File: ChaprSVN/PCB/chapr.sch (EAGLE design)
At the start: 30 parts, among them M2 RN42 Module, T1 3906, T2 3904

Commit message: Added power monitoring resistors. Fixed R15 label. Bumped to v1.1
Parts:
- removed C1, C2: (no value), resistor:CPOL-USE2.5-5
- added R16, R17: 24K, resistor:R-US_0207/10
- R15: value 10k -> 1.5k
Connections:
- new net N$31: ARDUINO.A6, R16.1, R17.2
- net +5V: no longer C1.+
- net GND: now also R16.2; no longer C1.-, C2.-
- net N$23: now also R17.1; no longer C2.+
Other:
- note added: "Power Monitor => A6"
- note added: "V 1.1"
- note removed: "V 1.0"
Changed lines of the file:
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@@
 <part name="R13" library="resistor" deviceset="R-US_" device="0207/10" value="10k"/>
 <part name="R14" library="resistor" deviceset="R-US_" device="0207/10" value="19.1k"/>
-<part name="R15" library="resistor" deviceset="R-US_" device="0207/10" value="10k"/>
+<part name="R15" library="resistor" deviceset="R-US_" device="0207/10" value="1.5k"/>
 <part name="D1" library="diode" deviceset="1N4148" device="DO35-7" value="1N4148"/>
 <part name="D2" library="diode" deviceset="1N4148" device="DO35-7" value="1N4148"/>
@@
 <part name="GND8" library="supply1" deviceset="GND" device=""/>
 <part name="U$3" library="ChapR-Custom" deviceset="VDIP2" device="BIGHOLE"/>
-<part name="C1" library="resistor" deviceset="CPOL-US" device="E2.5-5"/>
-<part name="C2" library="resistor" deviceset="CPOL-US" device="E2.5-5"/>
 <part name="GND9" library="supply1" deviceset="GND" device=""/>
-<part name="GND10" library="supply1" deviceset="GND" device=""/>
 <part name="T1" library="transistor-neu-to92" deviceset="*-PNP-" device="TO92-EBC" value="3906"/>
 <part name="T2" library="transistor-neu-to92" deviceset="*-NPN-" device="TO92-EBC" value="3904"/>
+<part name="R17" library="resistor" deviceset="R-US_" device="0207/10" value="24K"/>
+<part name="R16" library="resistor" deviceset="R-US_" device="0207/10" value="24K"/>
 </parts>
 <sheets>
@@
 <text x="81.026" y="18.796" size="1.778" layer="91">UART_TO_RN42</text>
 <text x="60.96" y="68.58" size="1.778" layer="91">UART_FROM_RN42</text>
-<text x="32.512" y="71.374" size="1.778" layer="91">Reset</text>
+<text x="45.212" y="71.374" size="1.778" layer="91">Reset</text>
 <wire x1="-83.82" y1="-30.48" x2="25.4" y2="-30.48" width="0.1524" layer="97"/>
 <wire x1="25.4" y1="-30.48" x2="25.4" y2="-76.2" width="0.1524" layer="97"/>
@@
 <text x="121.92" y="91.44" size="1.778" layer="97">*</text>
 <text x="111.506" y="125.222" size="1.778" layer="97">NOTE: 3.3v Comes from VDIP not ARD</text>
-<text x="162.56" y="-68.58" size="2.54" layer="97">V 1.0</text>
+<text x="162.56" y="-68.58" size="2.54" layer="97">V 1.1</text>
 <text x="76.2" y="-48.26" size="2.54" layer="97">ChapR Board</text>
-<text x="-5.08" y="-43.18" size="1.778" layer="97">Button  =&gt;  A0</text>
-<text x="-5.08" y="-48.26" size="1.778" layer="97">Speaker  &lt;=  A3</text>
-<text x="-5.08" y="-53.34" size="1.778" layer="97">Connect LED  &lt;=  A1</text>
-<text x="-5.08" y="-58.42" size="1.778" layer="97">Power LED  &lt;=  A2</text>
+<text x="-5.08" y="-37.338" size="1.778" layer="97">Button  =&gt;  A0</text>
+<text x="-5.08" y="-42.418" size="1.778" layer="97">Speaker  &lt;=  A3</text>
+<text x="-5.08" y="-47.498" size="1.778" layer="97">Connect LED  &lt;=  A1</text>
+<text x="-5.08" y="-52.578" size="1.778" layer="97">Power LED  &lt;=  A2</text>
 <text x="111.76" y="5.08" size="1.778" layer="91">Connected</text>
 <text x="4.318" y="125.476" size="1.778" layer="91" rot="R180">+</text>
@@
 <text x="49.022" y="79.502" size="1.778" layer="91">PowerHold</text>
 <text x="39.878" y="89.662" size="1.778" layer="91" rot="R90">SwitchMonitor</text>
-<text x="-5.08" y="-63.5" size="1.778" layer="97">Power Switch Mon =&gt; A5</text>
-<text x="-5.08" y="-66.548" size="1.778" layer="97">Power OFF &lt;= A4</text>
+<text x="-5.08" y="-57.658" size="1.778" layer="97">Power Switch Mon =&gt; A5</text>
+<text x="-5.334" y="-62.992" size="1.778" layer="97">Power OFF &lt;= A4</text>
 <text x="43.434" y="87.376" size="1.778" layer="91" rot="R90">(req's SW pull-up)</text>
+<text x="-5.588" y="-68.326" size="1.778" layer="95">Power Monitor =&gt; A6</text>
 </plain>
 <instances>
@@
 <instance part="ARDUINO" gate="G$1" x="2.54" y="55.88"/>
 <instance part="SUPPLY2" gate="G$1" x="-2.54" y="129.54"/>
-<instance part="GND4" gate="1" x="0" y="-12.7"/>
+<instance part="GND4" gate="1" x="-5.08" y="-10.16"/>
 <instance part="R9" gate="G$1" x="-50.8" y="2.54"/>
 <instance part="GND7" gate="1" x="-55.88" y="-20.32"/>
@@
 <instance part="GND8" gate="1" x="66.04" y="83.82"/>
 <instance part="U$3" gate="G$1" x="-55.88" y="50.8"/>
-<instance part="C1" gate="G$1" x="-33.02" y="124.46"/>
-<instance part="C2" gate="G$1" x="96.52" y="104.14"/>
-<instance part="GND9" gate="1" x="-25.4" y="114.3"/>
-<instance part="GND10" gate="1" x="96.52" y="96.52"/>
+<instance part="GND9" gate="1" x="35.56" y="-40.64"/>
 <instance part="T1" gate="G$1" x="83.82" y="114.3" smashed="yes">
 <attribute name="NAME" x="88.9" y="114.3" size="1.778" layer="95"/>
@@
 <attribute name="NAME" x="68.58" y="91.44" size="1.778" layer="95" rot="MR180"/>
 <attribute name="VALUE" x="68.58" y="93.98" size="1.778" layer="96" rot="MR180"/>
+</instance>
+<instance part="R17" gate="G$1" x="35.56" y="-7.62" smashed="yes" rot="R270">
+<attribute name="NAME" x="31.9786" y="-6.35" size="1.778" layer="95" rot="R270"/>
+<attribute name="VALUE" x="37.338" y="-6.35" size="1.778" layer="96" rot="R270"/>
+</instance>
+<instance part="R16" gate="G$1" x="35.56" y="-27.94" smashed="yes" rot="R270">
+<attribute name="NAME" x="31.9786" y="-26.67" size="1.778" layer="95" rot="R270"/>
+<attribute name="VALUE" x="37.338" y="-26.67" size="1.778" layer="96" rot="R270"/>
 </instance>
 </instances>
@@
 <wire x1="-12.7" y1="60.96" x2="-25.4" y2="60.96" width="0.1524" layer="91"/>
 <wire x1="-25.4" y1="60.96" x2="-25.4" y2="-5.08" width="0.1524" layer="91"/>
-<wire x1="-25.4" y1="-5.08" x2="0" y2="-5.08" width="0.1524" layer="91"/>
+<wire x1="-25.4" y1="-5.08" x2="-5.08" y2="-5.08" width="0.1524" layer="91"/>
 <pinref part="GND4" gate="1" pin="GND"/>
-<wire x1="0" y1="-5.08" x2="0" y2="-10.16" width="0.1524" layer="91"/>
-<junction x="0" y="-5.08"/>
+<wire x1="-5.08" y1="-5.08" x2="-5.08" y2="-7.62" width="0.1524" layer="91"/>
+<junction x="-5.08" y="-5.08"/>
 <pinref part="R10" gate="G$1" pin="1"/>
 <wire x1="27.94" y1="7.62" x2="27.94" y2="-5.08" width="0.1524" layer="91"/>
 <wire x1="27.94" y1="-5.08" x2="25.4" y2="-5.08" width="0.1524" layer="91"/>
 <pinref part="ARDUINO" gate="G$1" pin="GND2"/>
-<wire x1="25.4" y1="-5.08" x2="0" y2="-5.08" width="0.1524" layer="91"/>
+<wire x1="25.4" y1="-5.08" x2="-5.08" y2="-5.08" width="0.1524" layer="91"/>
 <wire x1="15.24" y1="66.04" x2="25.4" y2="66.04" width="0.1524" layer="91"/>
 <wire x1="25.4" y1="66.04" x2="25.4" y2="-5.08" width="0.1524" layer="91"/>
@@
 </segment>
 <segment>
-<pinref part="C1" gate="G$1" pin="-"/>
-<wire x1="-33.02" y1="119.38" x2="-25.4" y2="119.38" width="0.1524" layer="91"/>
 <pinref part="GND9" gate="1" pin="GND"/>
-<wire x1="-25.4" y1="119.38" x2="-25.4" y2="116.84" width="0.1524" layer="91"/>
-</segment>
-<segment>
-<pinref part="C2" gate="G$1" pin="-"/>
-<pinref part="GND10" gate="1" pin="GND"/>
+<pinref part="R16" gate="G$1" pin="2"/>
+<wire x1="35.56" y1="-38.1" x2="35.56" y2="-33.02" width="0.1524" layer="91"/>
 </segment>
 </net>
@@
 <pinref part="M2" gate="G$1" pin="UARTTX"/>
 <wire x1="106.68" y1="68.58" x2="101.6" y2="68.58" width="0.1524" layer="91"/>
-<wire x1="101.6" y1="68.58" x2="33.02" y2="68.58" width="0.1524" layer="91"/>
-<wire x1="33.02" y1="68.58" x2="33.02" y2="45.72" width="0.1524" layer="91"/>
+<wire x1="101.6" y1="68.58" x2="38.1" y2="68.58" width="0.1524" layer="91"/>
+<wire x1="38.1" y1="68.58" x2="38.1" y2="45.72" width="0.1524" layer="91"/>
 <pinref part="ARDUINO" gate="G$1" pin="D12"/>
-<wire x1="33.02" y1="45.72" x2="15.24" y2="45.72" width="0.1524" layer="91"/>
+<wire x1="38.1" y1="45.72" x2="15.24" y2="45.72" width="0.1524" layer="91"/>
 </segment>
 </net>
@@
 <pinref part="U$3" gate="G$1" pin="5.0V(2)"/>
 <pinref part="U$3" gate="G$1" pin="5.0V(3)"/>
-<wire x1="-33.02" y1="127" x2="-43.18" y2="127" width="0.1524" layer="91"/>
-<junction x="-43.18" y="127"/>
-<pinref part="C1" gate="G$1" pin="+"/>
 </segment>
 </net>
@@
 <segment>
 <pinref part="ARDUINO" gate="G$1" pin="RAWV"/>
-<wire x1="17.78" y1="76.2" x2="17.78" y2="68.58" width="0.1524" layer="91"/>
-<wire x1="17.78" y1="68.58" x2="15.24" y2="68.58" width="0.1524" layer="91"/>
+<wire x1="35.56" y1="76.2" x2="35.56" y2="68.58" width="0.1524" layer="91"/>
+<wire x1="35.56" y1="68.58" x2="15.24" y2="68.58" width="0.1524" layer="91"/>
 <wire x1="86.36" y1="109.22" x2="86.36" y2="106.68" width="0.1524" layer="91"/>
 <wire x1="86.36" y1="106.68" x2="86.36" y2="76.2" width="0.1524" layer="91"/>
-<wire x1="86.36" y1="76.2" x2="17.78" y2="76.2" width="0.1524" layer="91"/>
-<pinref part="C2" gate="G$1" pin="+"/>
-<wire x1="96.52" y1="106.68" x2="86.36" y2="106.68" width="0.1524" layer="91"/>
-<junction x="86.36" y="106.68"/>
+<wire x1="86.36" y1="76.2" x2="35.56" y2="76.2" width="0.1524" layer="91"/>
 <pinref part="T1" gate="G$1" pin="C"/>
+<junction x="35.56" y="68.58"/>
+<pinref part="R17" gate="G$1" pin="1"/>
+<wire x1="35.56" y1="68.58" x2="35.56" y2="-2.54" width="0.1524" layer="91"/>
 </segment>
 </net>
@@
 </segment>
 </net>
+<net name="N$31" class="0">
+<segment>
+<pinref part="ARDUINO" gate="G$1" pin="A6"/>
+<wire x1="2.54" y1="25.4" x2="2.54" y2="-12.7" width="0.1524" layer="91"/>
+<wire x1="2.54" y1="-12.7" x2="20.32" y2="-12.7" width="0.1524" layer="91"/>
+<pinref part="R17" gate="G$1" pin="2"/>
+<wire x1="20.32" y1="-12.7" x2="35.56" y2="-12.7" width="0.1524" layer="91"/>
+<junction x="35.56" y="-12.7"/>
+<pinref part="R16" gate="G$1" pin="1"/>
+<wire x1="35.56" y1="-12.7" x2="35.56" y2="-22.86" width="0.1524" layer="91"/>
+</segment>
+</net>

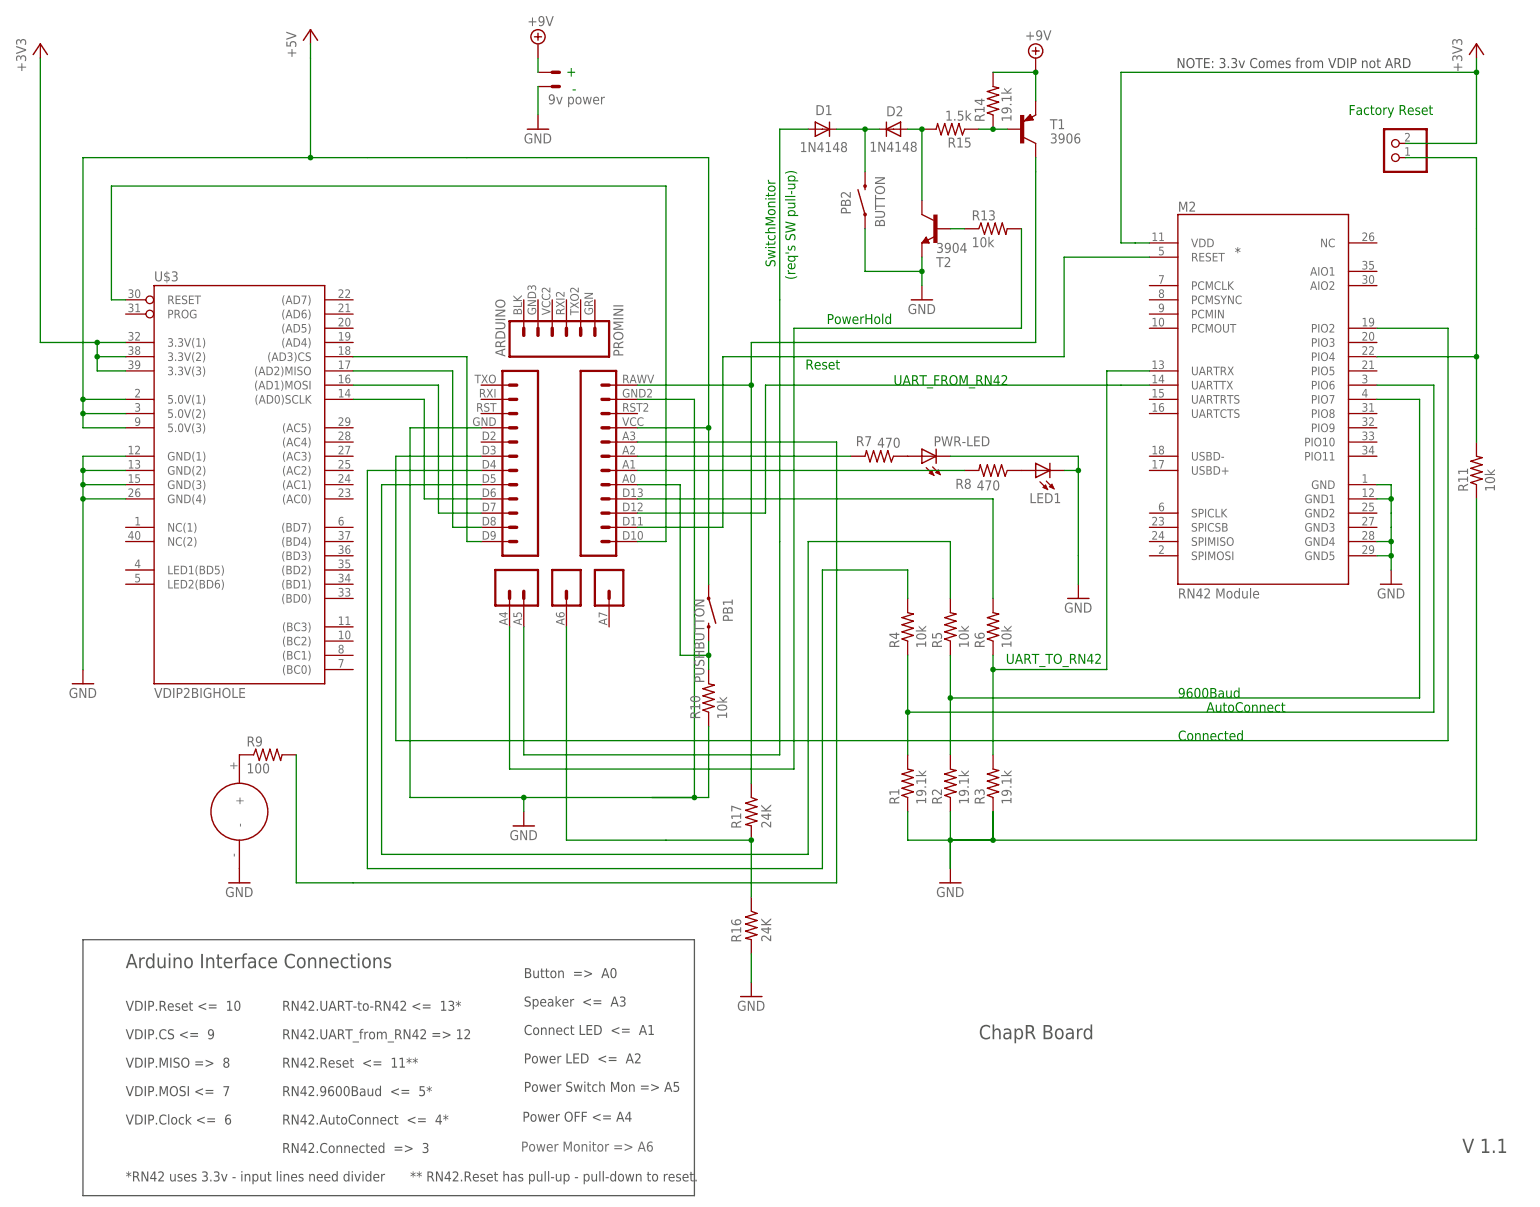
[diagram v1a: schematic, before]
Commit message: 
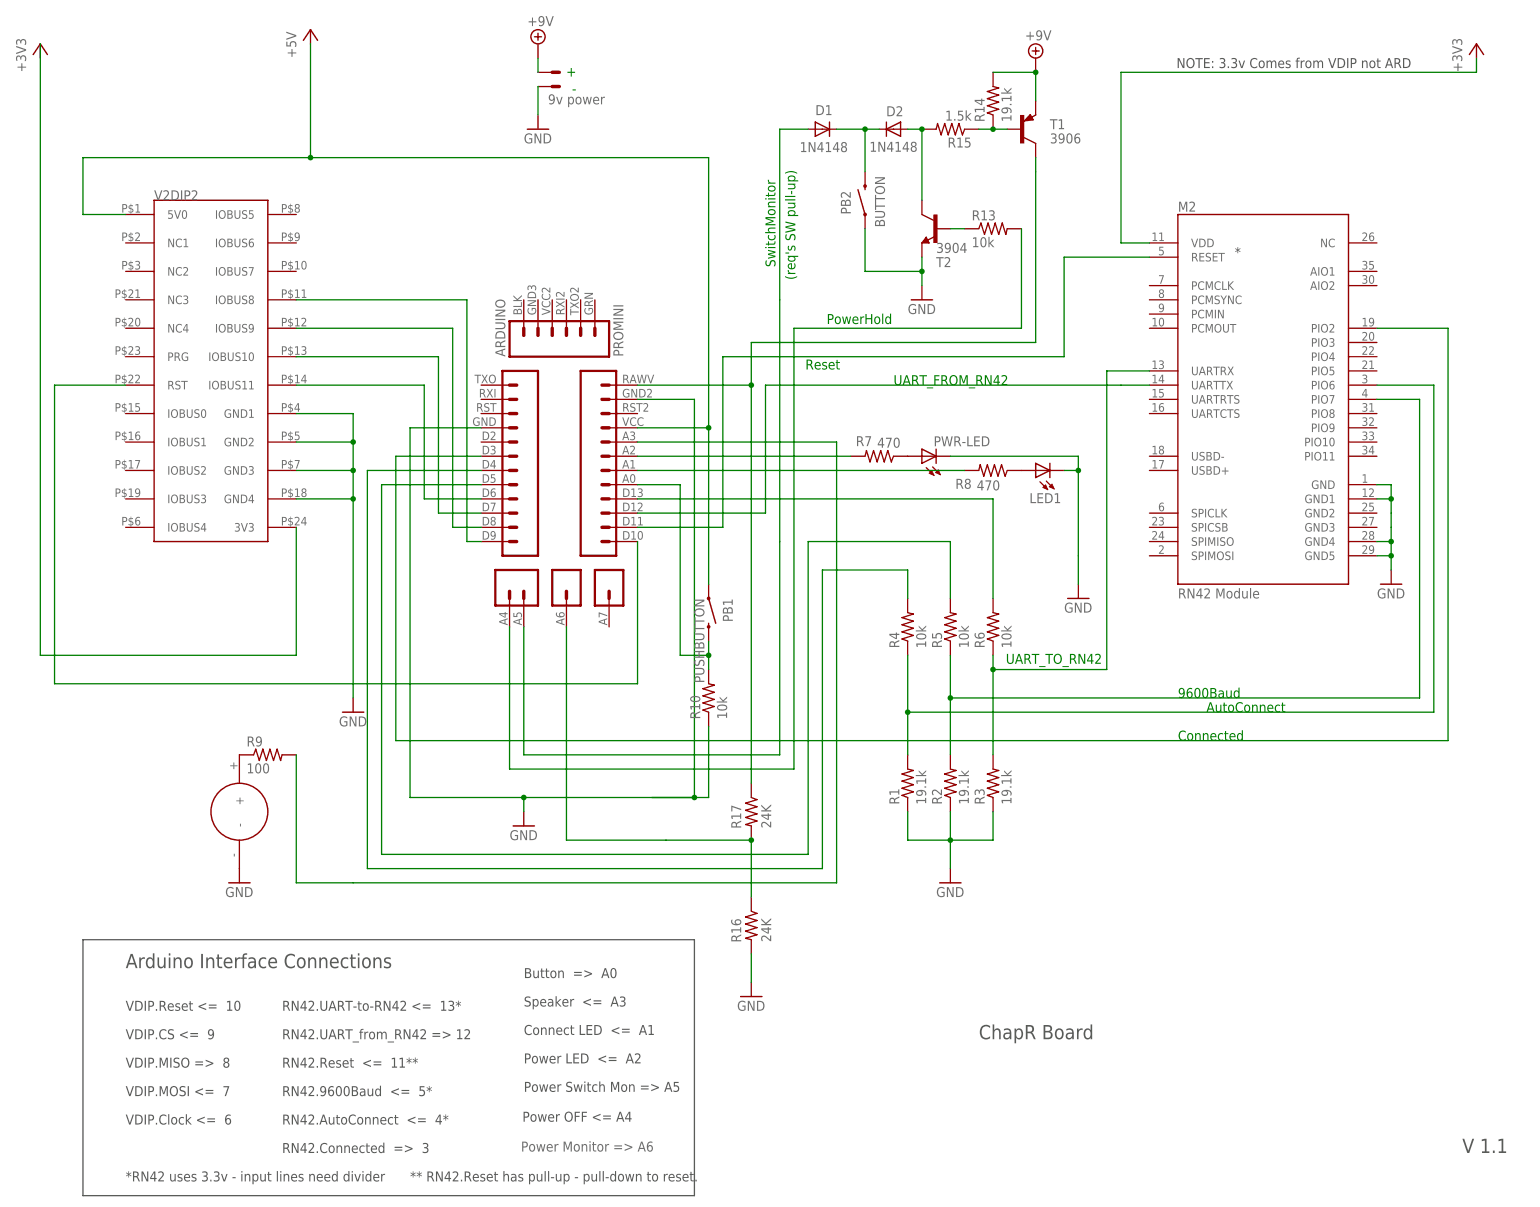
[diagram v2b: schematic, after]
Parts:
- removed JP1: (no value), pinhead:PINHD-1X2
- removed R11: 10k, resistor:R-US_0207/10
- removed U$3: VDIP2BIGHOLE, ChapR-Custom:VDIP2BIGHOLE
- added V2DIP2: V2DIP2, ChapR-Custom:V2DIP2
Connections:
- removed net N$22: JP1.1, M2.PIO4, R11.2
- new net N$28: V2DIP2.3V3
- net +3V3: no longer JP1.2, U$3.3.3V(1), U$3.3.3V(2), U$3.3.3V(3)
- net +5V: now also V2DIP2.5V0; no longer U$3.5.0V(1), U$3.5.0V(2), U$3.5.0V(3)
- net GND: now also V2DIP2.GND1, V2DIP2.GND2, V2DIP2.GND3, V2DIP2.GND4; no longer R11.1, U$3.GND(1), U$3.GND(2), U$3.GND(3), U$3.GND(4)
- net N$10: now also ARDUINO.D6, V2DIP2.IOBUS11; no longer ARDUINO.D9, U$3.(AD3)CS
- net N$11: now also ARDUINO.D7, V2DIP2.IOBUS10; no longer ARDUINO.D8, U$3.(AD2)MISO
- net N$12: now also ARDUINO.D8, V2DIP2.IOBUS9; no longer ARDUINO.D7, U$3.(AD1)MOSI
- net N$13: now also ARDUINO.D9, V2DIP2.IOBUS8; no longer ARDUINO.D6, U$3.(AD0)SCLK
- net N$2: now also V2DIP2.RST; no longer U$3.RESET
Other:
- note removed: "Factory Reset"

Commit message: 
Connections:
- removed net N$28: V2DIP2.3V3
- net +3V3: now also V2DIP2.3V3
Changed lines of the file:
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@@
 <wire x1="165.1" y1="124.46" x2="165.1" y2="127" width="0.1524" layer="91"/>
+</segment>
+<segment>
+<wire x1="-91.44" y1="129.54" x2="-91.44" y2="20.32" width="0.1524" layer="91"/>
+<wire x1="-91.44" y1="20.32" x2="-45.72" y2="20.32" width="0.1524" layer="91"/>
+<pinref part="V2DIP2" gate="G$1" pin="3V3"/>
+<wire x1="-45.72" y1="20.32" x2="-45.72" y2="43.18" width="0.1524" layer="91"/>
 </segment>
 </net>
@@
 </segment>
 </net>
-<net name="N$28" class="0">
-<segment>
-<wire x1="-91.44" y1="129.54" x2="-91.44" y2="20.32" width="0.1524" layer="91"/>
-<wire x1="-91.44" y1="20.32" x2="-45.72" y2="20.32" width="0.1524" layer="91"/>
-<pinref part="V2DIP2" gate="G$1" pin="3V3"/>
-<wire x1="-45.72" y1="20.32" x2="-45.72" y2="43.18" width="0.1524" layer="91"/>
-</segment>
-</net>

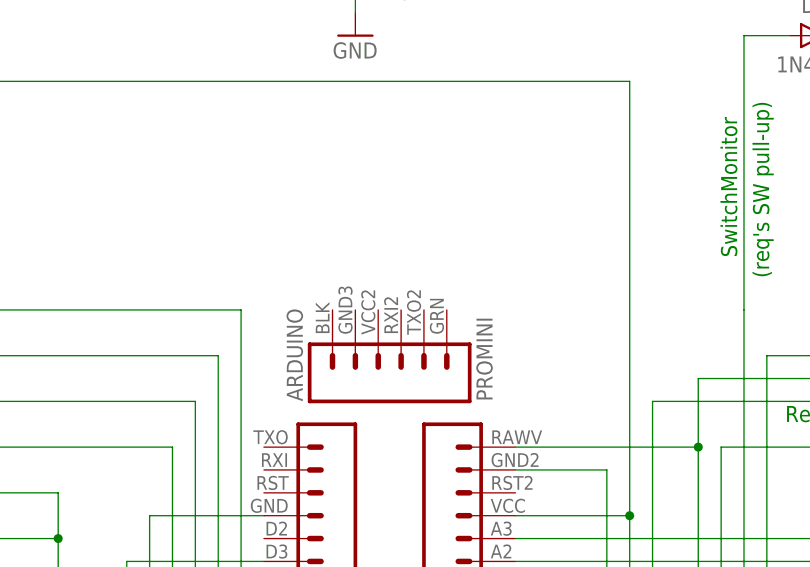
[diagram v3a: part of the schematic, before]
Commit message: Used the new ProMini without the top 6 pins. Created AutoRouter and DesignRule files for repeatable routing. Added clearance between vias and pads so we don't have to post-process the routes.
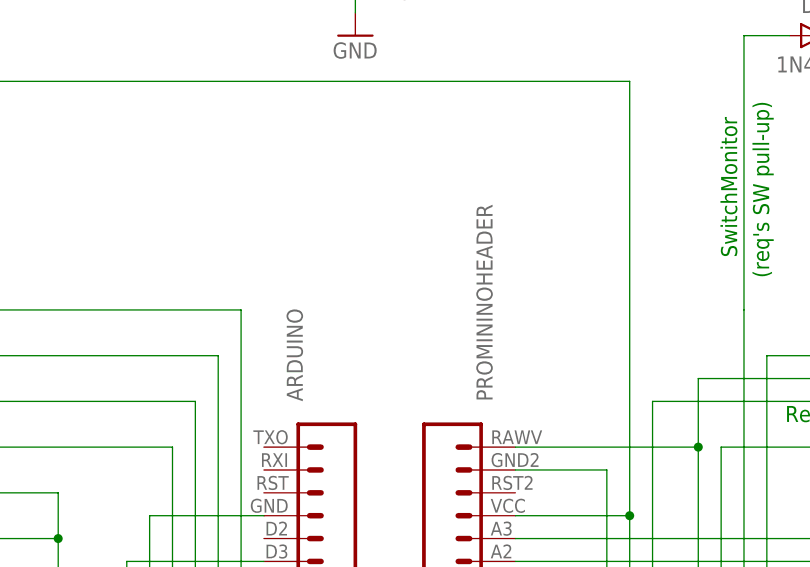
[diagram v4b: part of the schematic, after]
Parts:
- ARDUINO: value PROMINI -> PROMININOHEADER; device ChapR-Custom:PROMINI -> ChapR-Custom:PROMININOHEADER
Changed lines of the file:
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@@
 <part name="R7" library="resistor" deviceset="R-US_" device="0207/10" value="470"/>
 <part name="R8" library="resistor" deviceset="R-US_" device="0207/10" value="470"/>
-<part name="ARDUINO" library="ChapR-Custom" deviceset="PROMINI" device=""/>
+<part name="ARDUINO" library="ChapR-Custom" deviceset="PROMININOHEADER" device=""/>
 <part name="SUPPLY2" library="supply2" deviceset="+9V" device=""/>
 <part name="GND4" library="supply1" deviceset="GND" device=""/>
